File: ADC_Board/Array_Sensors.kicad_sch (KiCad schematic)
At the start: 30 parts, among them U1 OPA990IDCKR, U2 OPA990IDCKR, U3 INA210AIDCKR, U4 INA210AIDCKR

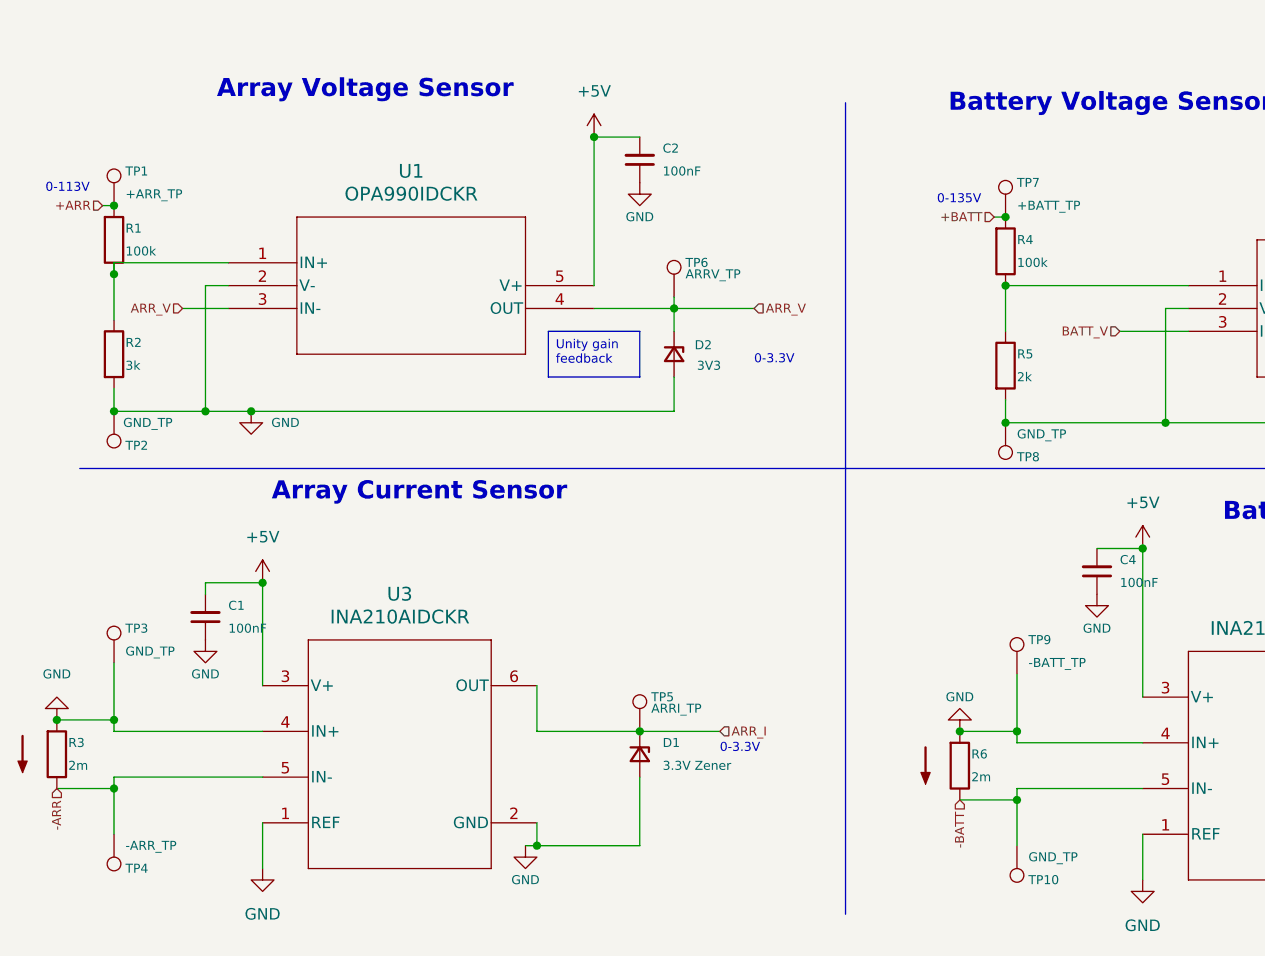
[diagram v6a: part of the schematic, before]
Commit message: final iteration of schematic before printing
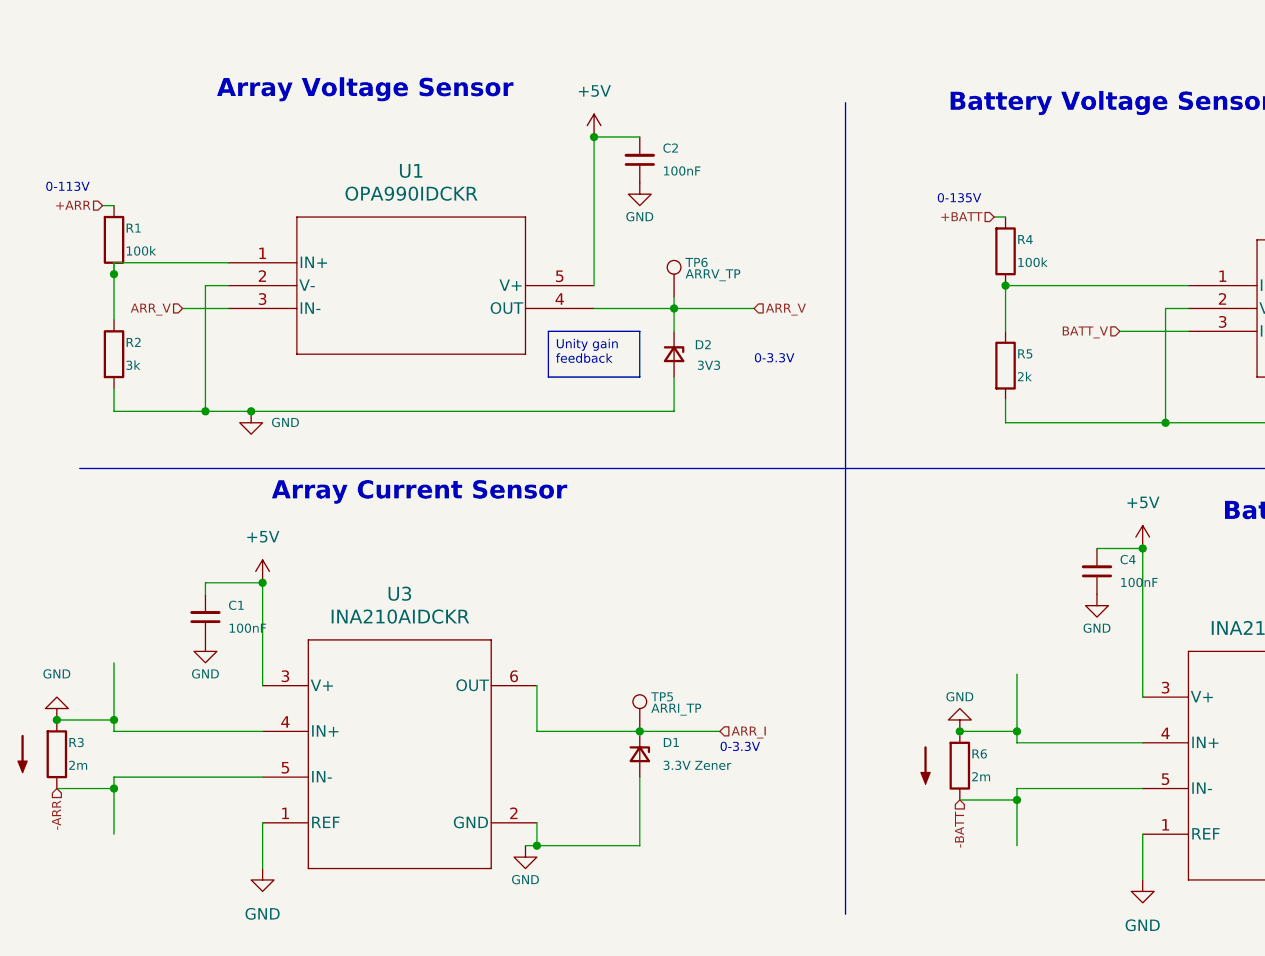
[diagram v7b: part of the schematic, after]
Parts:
- removed TP1: +ARR_TP, UTSVT_Special:TestPoint_HEX_3mmID, symbol Connector:TestPoint
- removed TP10, TP2, TP3, TP8: GND_TP, UTSVT_Special:TestPoint_HEX_3mmID, symbol Connector:TestPoint
- removed TP4: -ARR_TP, UTSVT_Special:TestPoint_HEX_3mmID, symbol Connector:TestPoint
- removed TP7: +BATT_TP, UTSVT_Special:TestPoint_HEX_3mmID, symbol Connector:TestPoint
- removed TP9: -BATT_TP, UTSVT_Special:TestPoint_HEX_3mmID, symbol Connector:TestPoint

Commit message: made changes to layout and schematic
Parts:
- R1, R2, R4, R5: footprint Resistor_SMD:R_0805_2012Metric -> Resistor_SMD:R_1206_3216Metric_Pad1.30x1.75mm_HandSolder
- R3, R6: footprint Resistor_THT:R_Axial_Power_L20.0mm_W6.4mm_P30.48mm -> Resistor_SMD:R_1206_3216Metric
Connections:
- net +ARR renamed +ARR_IN
- net +BATT renamed BATT+_IN
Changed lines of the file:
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@@
 	(text "0-135V"
 		(exclude_from_sim no)
-		(at 166.37 59.69 0)
+		(at 166.624 58.42 0)
 		(effects
 			(font
@@
 		)
 	)
-	(hierarchical_label "+BATT"
+	(hierarchical_label "ARR_I"
 		(shape input)
-		(at 172.72 60.96 180)
+		(at 142.24 118.11 0)
 		(fields_autoplaced yes)
 		(effects
@@
 				(size 1 1)
 			)
-			(justify right)
+			(justify left)
 		)
 	)
-	(hierarchical_label "ARR_I"
+	(hierarchical_label "ARR_V"
 		(shape input)
-		(at 142.24 118.11 0)
+		(at 146.05 71.12 0)
 		(fields_autoplaced yes)
 		(effects
@@
 		)
 	)
-	(hierarchical_label "ARR_V"
+	(hierarchical_label "BATT+_IN"
 		(shape input)
-		(at 146.05 71.12 0)
+		(at 172.72 60.96 180)
 		(fields_autoplaced yes)
 		(effects
 			(font
-				(size 1 1)
+				(size 1.27 1.27)
 			)
-			(justify left)
+			(justify right)
 		)
 	)
@@
 		)
 	)
-	(hierarchical_label "+ARR"
+	(hierarchical_label "+ARR_IN"
 		(shape input)
 		(at 73.66 59.69 180)
@@
 			)
 		)
-		(property "Footprint" "Resistor_SMD:R_0805_2012Metric"
+		(property "Footprint" "Resistor_SMD:R_1206_3216Metric_Pad1.30x1.75mm_HandSolder"
 			(at 172.212 64.77 90)
 			(effects
@@
 			)
 		)
-		(property "Footprint" "Resistor_SMD:R_0805_2012Metric"
+		(property "Footprint" "Resistor_SMD:R_1206_3216Metric_Pad1.30x1.75mm_HandSolder"
 			(at 172.212 77.47 90)
 			(effects
@@
 			)
 		)
-		(property "Footprint" "Resistor_SMD:R_0805_2012Metric"
+		(property "Footprint" "Resistor_SMD:R_1206_3216Metric_Pad1.30x1.75mm_HandSolder"
 			(at 73.152 76.2 90)
 			(effects
@@
 			)
 		)
-		(property "Footprint" "Resistor_SMD:R_0805_2012Metric"
+		(property "Footprint" "Resistor_SMD:R_1206_3216Metric_Pad1.30x1.75mm_HandSolder"
 			(at 73.152 63.5 90)
 			(effects
@@
 			)
 		)
-		(property "Footprint" "Resistor_THT:R_Axial_Power_L20.0mm_W6.4mm_P30.48mm"
+		(property "Footprint" "Resistor_SMD:R_1206_3216Metric"
 			(at 167.132 121.92 90)
 			(effects
@@
 			)
 		)
-		(property "Footprint" "Resistor_THT:R_Axial_Power_L20.0mm_W6.4mm_P30.48mm"
+		(property "Footprint" "Resistor_SMD:R_1206_3216Metric"
 			(at 66.802 120.65 90)
 			(effects
